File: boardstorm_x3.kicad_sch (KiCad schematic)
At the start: 41 parts, among them J1 USB_C_Receptacle_USB2.0_14P, J2 Conn_01x20_Pin, J3 Conn_01x20_Pin, J4 Conn_01x03_Pin, SW1 SW_Push, U1 RP2040, U2 MCP1700x-330xxTT, U3 W25Q16JVSS, U4 BQ24075RGT, Y1 12 MHz

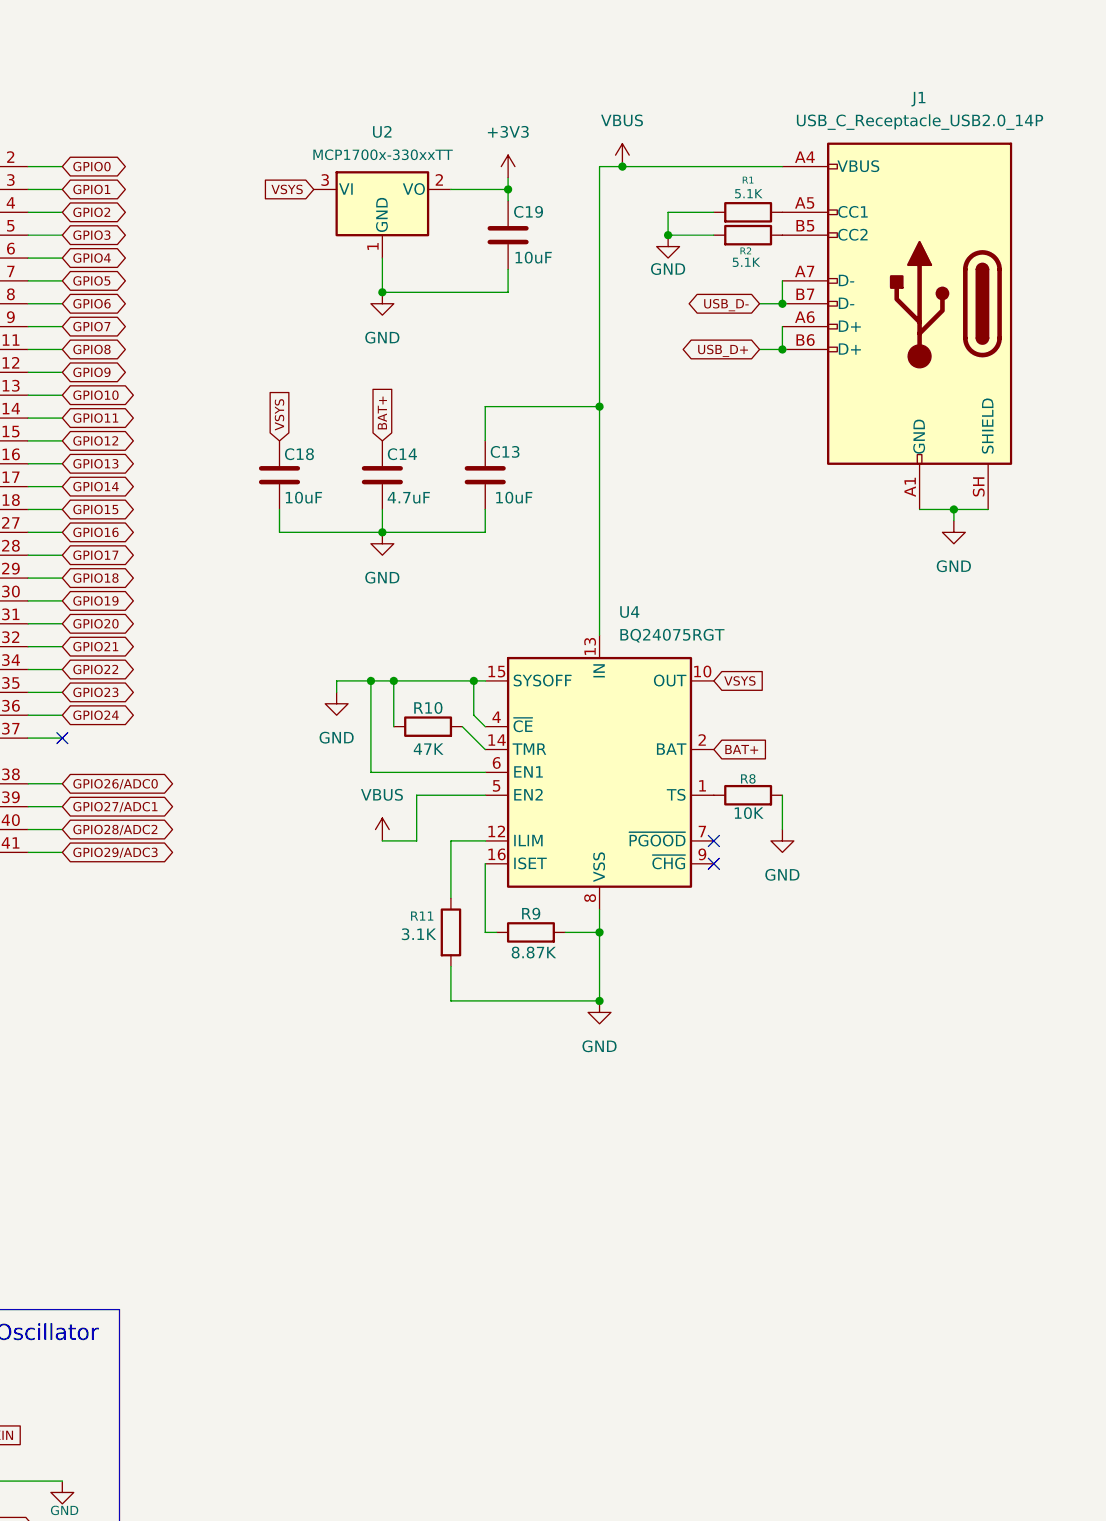
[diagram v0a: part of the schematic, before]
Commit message: added the fuel gauge, any assets related to it, and journal
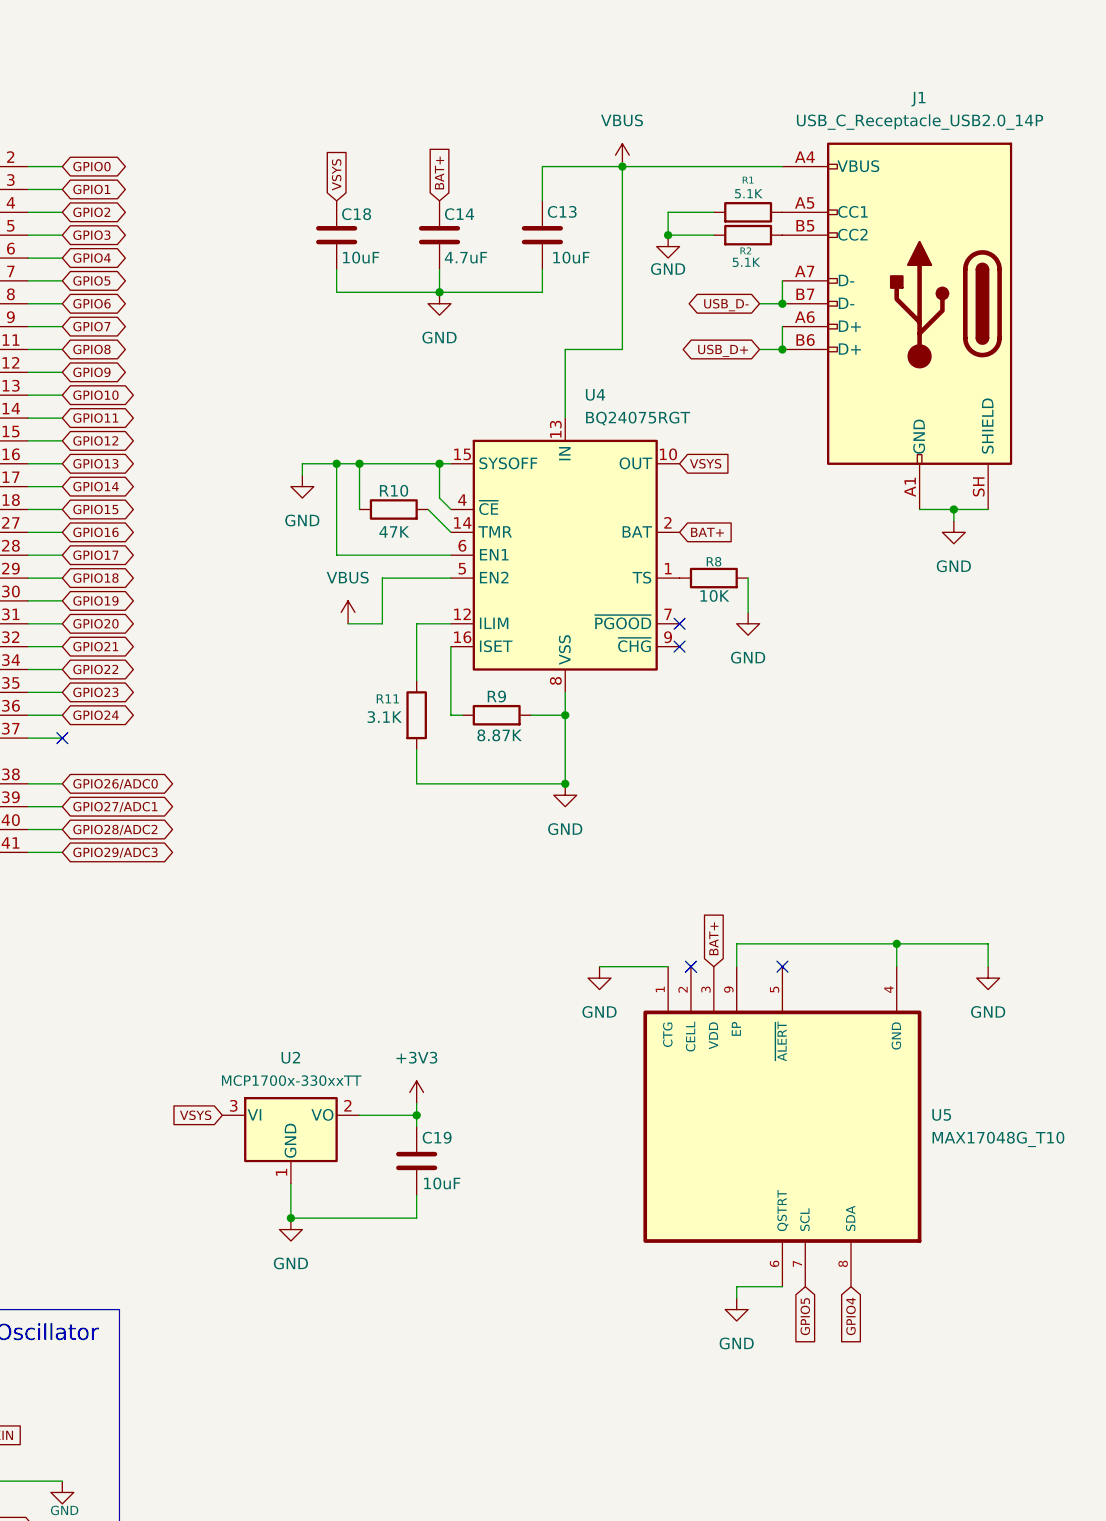
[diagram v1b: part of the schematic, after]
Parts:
- added U5: MAX17048G_T10, MAX17048G_T10:SON50P200X200X80-9N, symbol MAX17048G_T10:MAX17048G_T10
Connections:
- net BAT+: now also U5.3 (VDD)
- net GND: now also U5.1 (CTG), U5.4 (GND), U5.6 (QSTRT), U5.9 (EP)
- net GPIO4: now also U5.8 (SDA)
- net GPIO5: now also U5.7 (SCL)
- no-connect marks 3 -> 5
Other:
- moved on the sheet: C13, C14, C18, C19, R10, R11, R8, R9, U2, U4

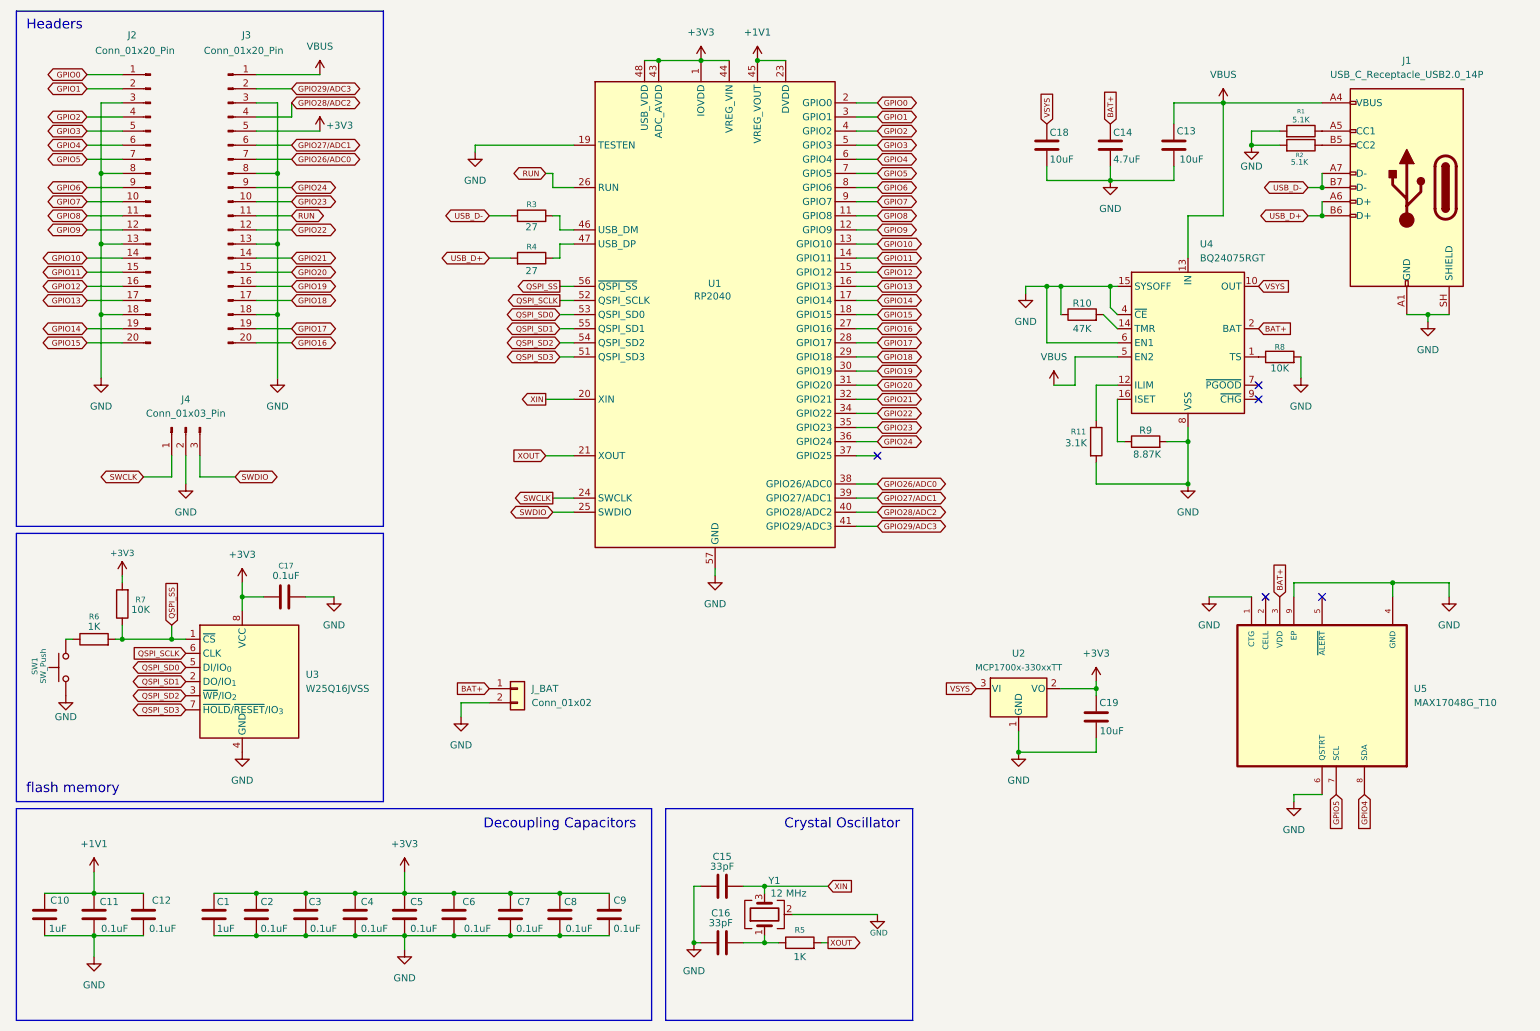
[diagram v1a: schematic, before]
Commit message: fixing a bunch of ERC issues
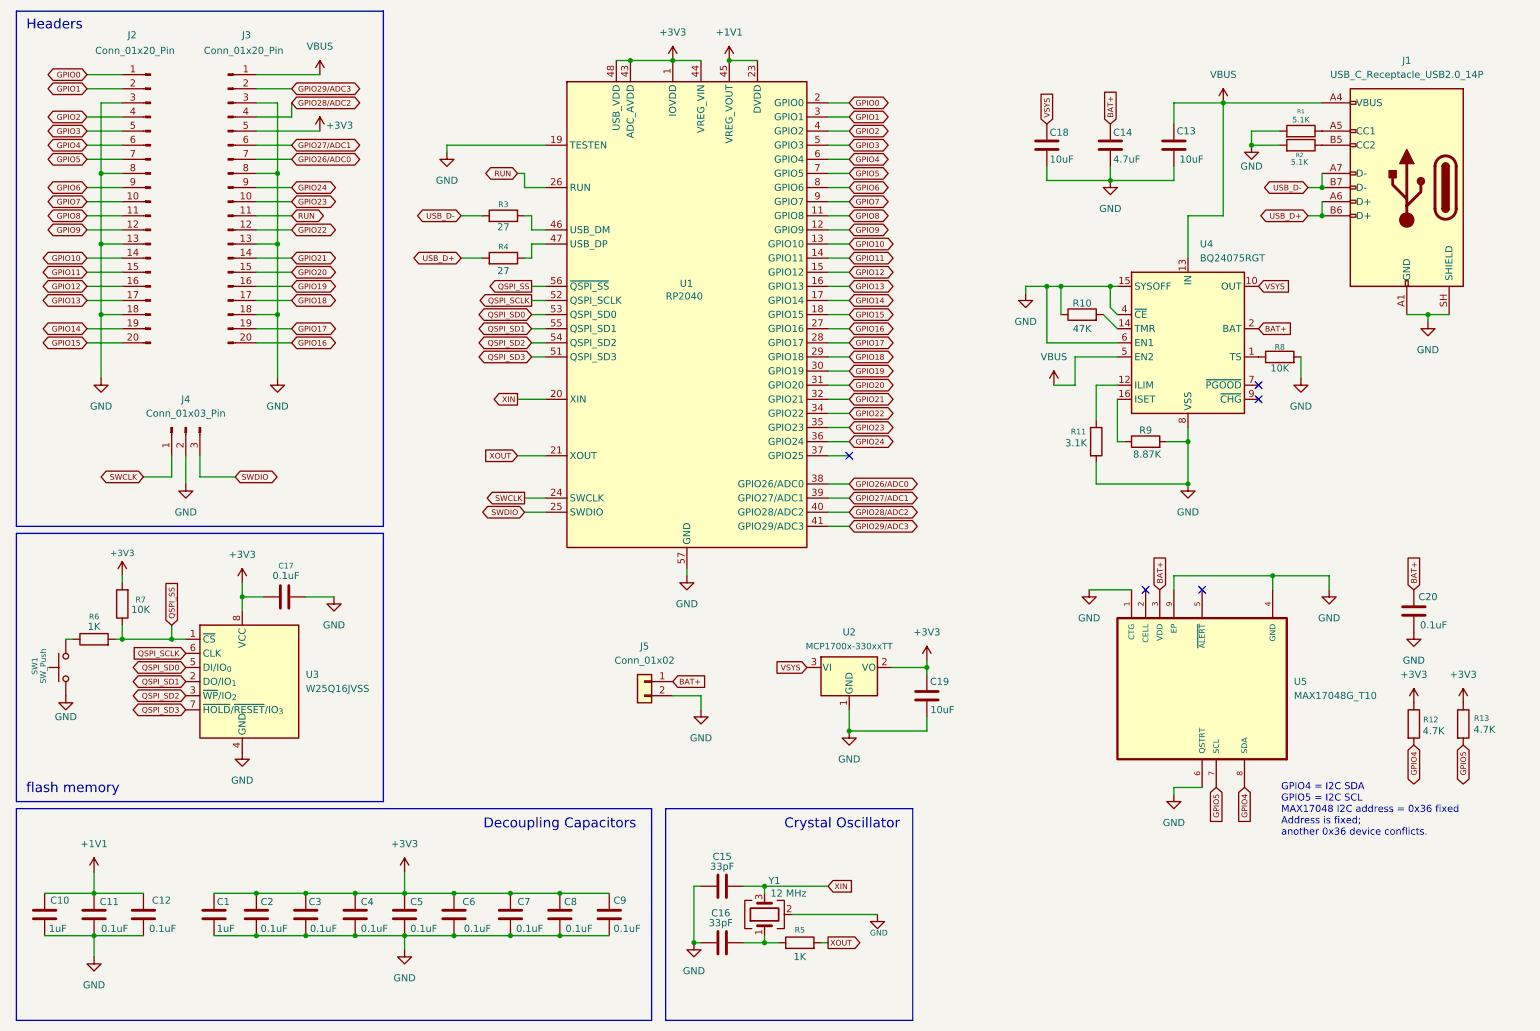
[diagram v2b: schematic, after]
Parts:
- added C20: 0.1uF, symbol Device:C
- added R12, R13: 4.7K, symbol Device:R
- renumbered J_BAT to J5
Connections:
- net +3V3: now also R12.1, R13.1
- net BAT+: now also C20.1
- net GND: now also C20.2
- net GPIO4: now also R12.2
- net GPIO5: now also R13.2
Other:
- note added: "GPIO4 = I2C SDA GPIO5 = I2C SCL MAX17048 I2C address = 0x36 fixed Address is fixed; another 0x36 device conflicts."
- moved on the sheet: C19, J5, R3, R4, U1, U2, U5

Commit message: organized schematic design,, added some notes to readme, updated journal
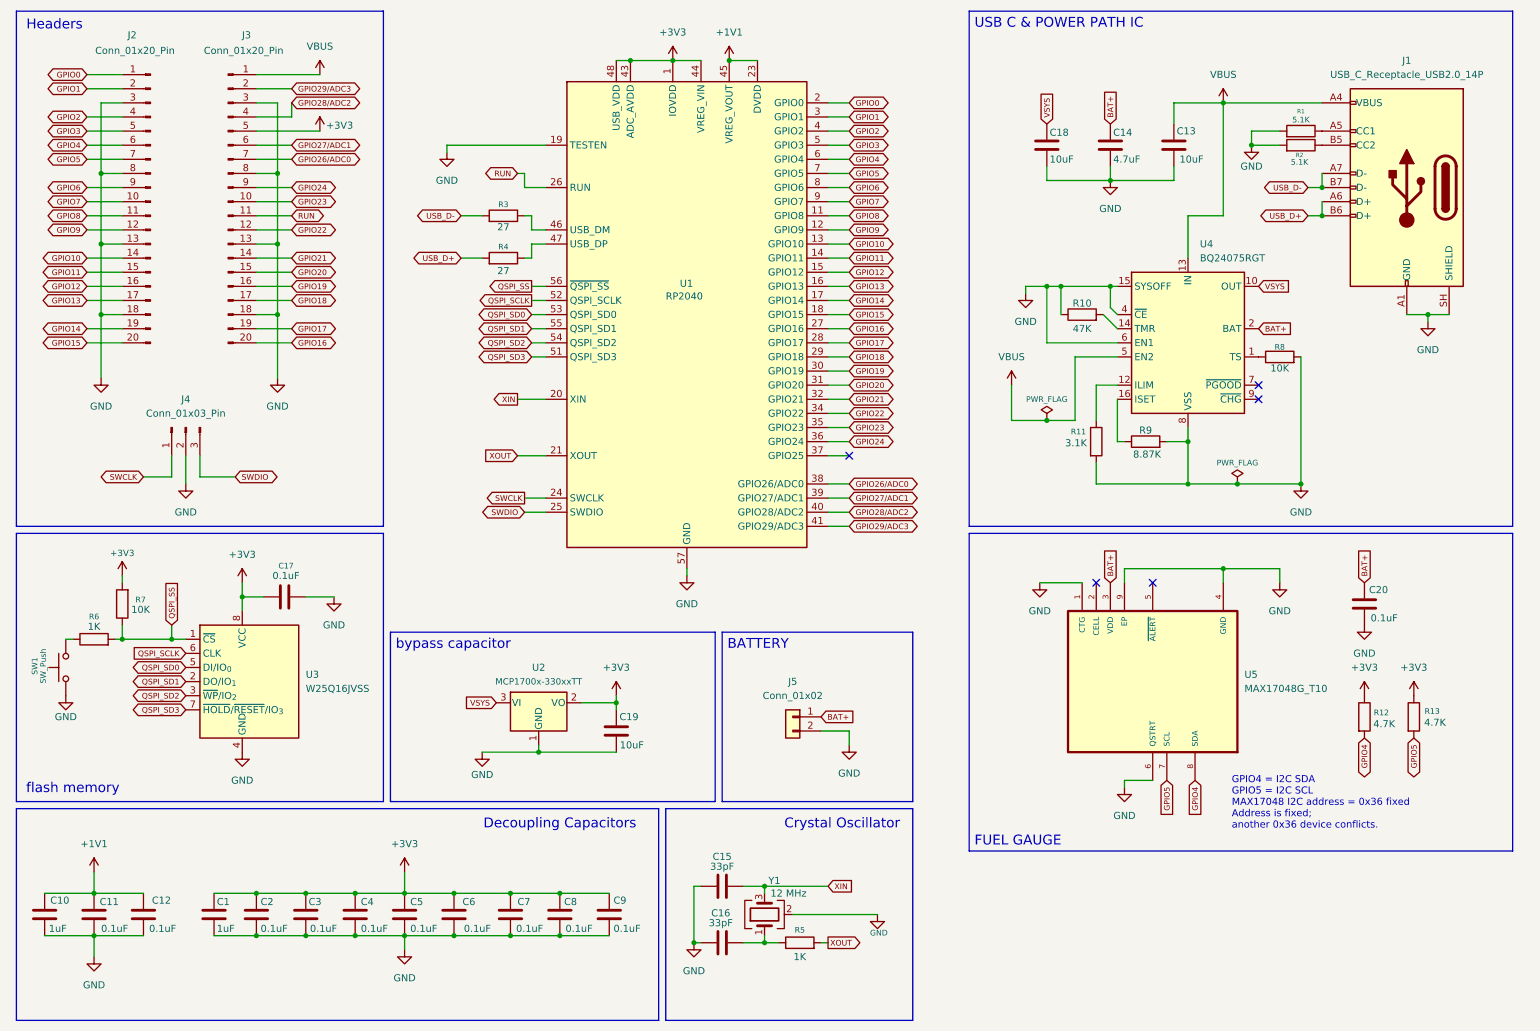
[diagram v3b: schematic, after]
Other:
- moved on the sheet: C19, C20, J5, R12, R13, U2, U5
